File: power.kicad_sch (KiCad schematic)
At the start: 11 parts, among them IC1 AP63203WU-7, J1 Barrel_Jack_Switch_Pin3Ring

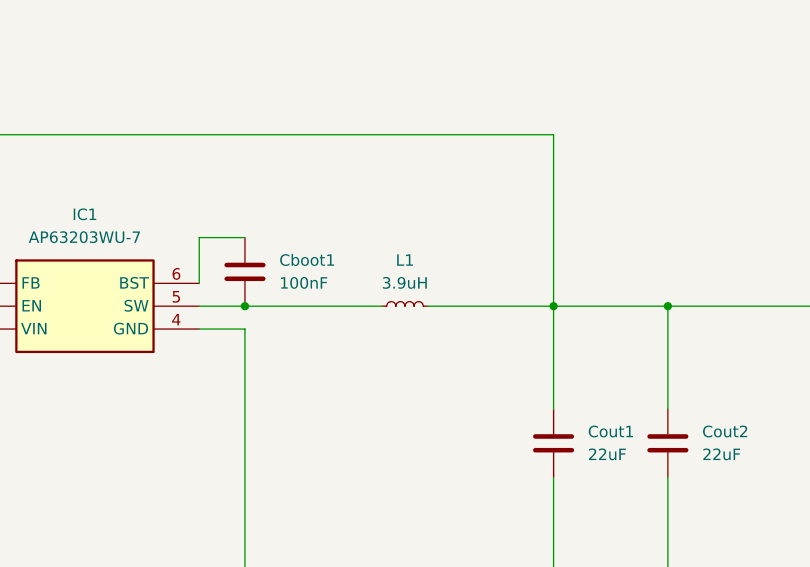
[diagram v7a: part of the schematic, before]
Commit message: fix: FP for USB connector and schotky diode
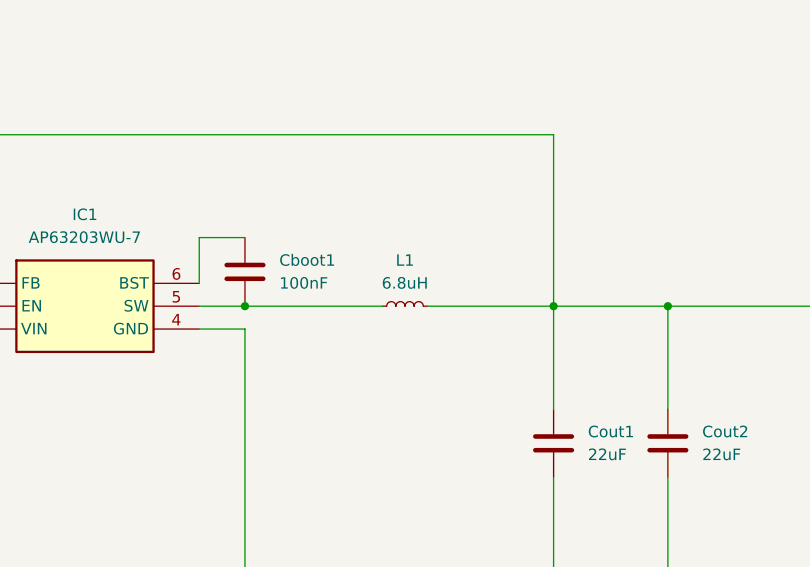
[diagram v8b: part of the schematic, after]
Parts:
- D2, D3: footprint Diode_THT:D_T-1_P10.16mm_Horizontal -> schotky_DB2441600L:SODFL4724X90N
- L1: value 3.9uH -> 6.8uH; footprint Inductor_SMD:L_Bourns-SRN6028 -> Inductor_SMD:L_Bourns_SRR1260
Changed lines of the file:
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@@
 			)
 		)
-		(property "Footprint" "Diode_THT:D_T-1_P10.16mm_Horizontal"
+		(property "Footprint" "schotky_DB2441600L:SODFL4724X90N"
 			(at 113.03 62.23 90)
 			(effects
@@
 			)
 		)
-		(property "Footprint" "Diode_THT:D_T-1_P10.16mm_Horizontal"
+		(property "Footprint" "schotky_DB2441600L:SODFL4724X90N"
 			(at 102.87 68.58 90)
 			(effects
@@
 			)
 		)
-		(property "Value" "3.9uH"
+		(property "Value" "6.8uH"
 			(at 189.23 63.5 90)
 			(effects
@@
 			)
 		)
-		(property "Footprint" "Inductor_SMD:L_Bourns-SRN6028"
+		(property "Footprint" "Inductor_SMD:L_Bourns_SRR1260"
 			(at 189.23 66.04 0)
 			(effects
